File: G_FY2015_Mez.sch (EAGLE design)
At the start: 197 parts, among them IC100 FT232RL, J1 RPI2_GPIO_HOLES, J100 EPL.00.250.NTN, J101 EPL.00.250.NTN, J102 EPL.00.250.NTN, J103 EPL.00.250.NTN, J180 TOKUDEN_SP6, J181 USB Mini-B Connector, J2 SPACEWIRE_MDMMDM9, J300 SHV_PIGTAIL_LAND, J301 SHV_PIGTAIL_LAND, J600_12V IL-4P-S3EN2, J610 2.1MMJACKTHM, U10 LM60, U100 AD9215, U101 AD8138, U102 LM6142, U11 MCP4822-E/SN, U110 AD9215, U111 AD8138, U112 LM6142, U120 AD9215, U121 AD8138, U122 LM6142, U130 AD9215, U131 AD8138, U132 LM6142, U190 SN65LVDS049, U191 GPS_FGPMMOPA6H, U192 LED-5, U300 OPTON_1PA_12, U301 OPTON_1PA_12, U302 2SC1815, U303 2SJ313, U5 MCP3208-CI/SL, U500 LT6106, U510 LT6106, U6 MCP1525TSOT-23-3, U600 PHT12050WAH, U610 PHT12050WAH, U620 LTC1983ES6-3, U7 LM60, U8 LM60, U9 LM60

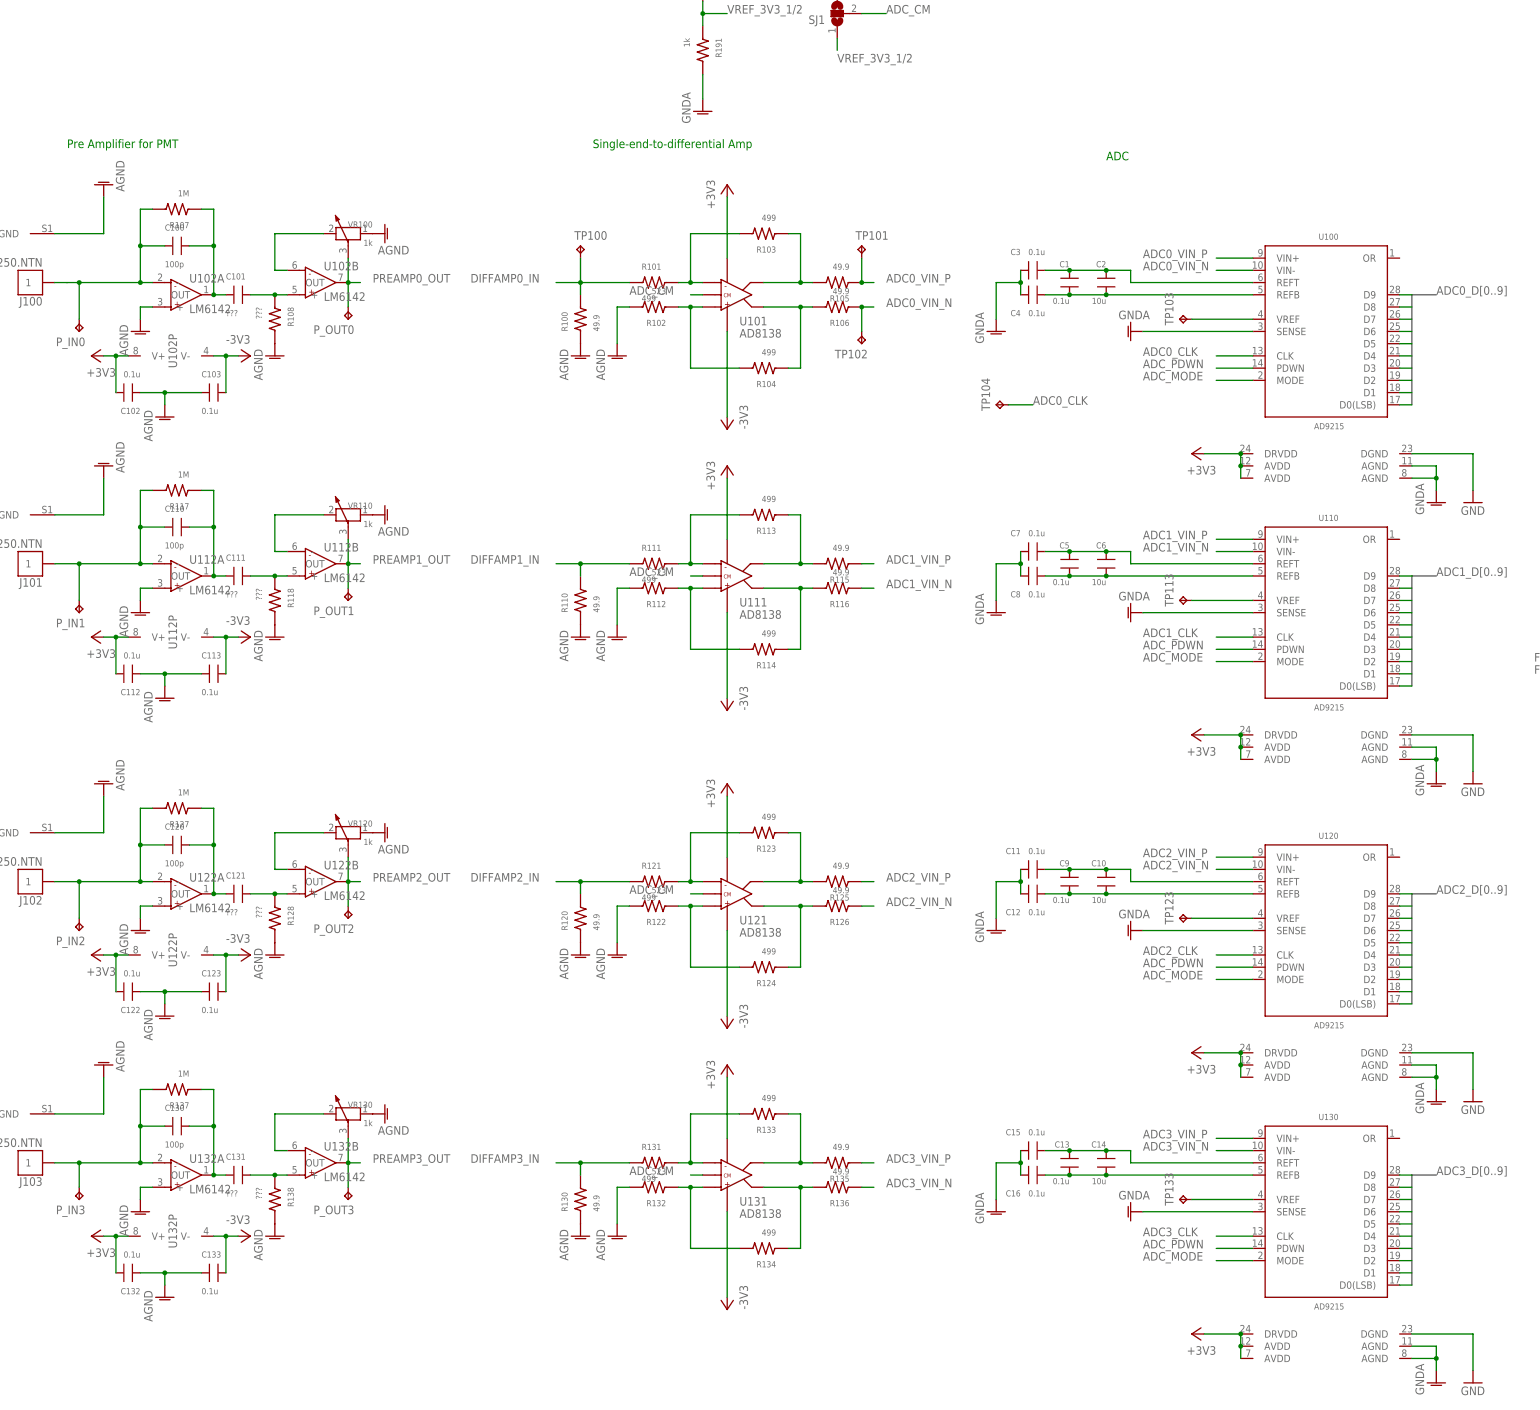
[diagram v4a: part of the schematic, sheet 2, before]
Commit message: GNDA and AGND removed (just use GND)
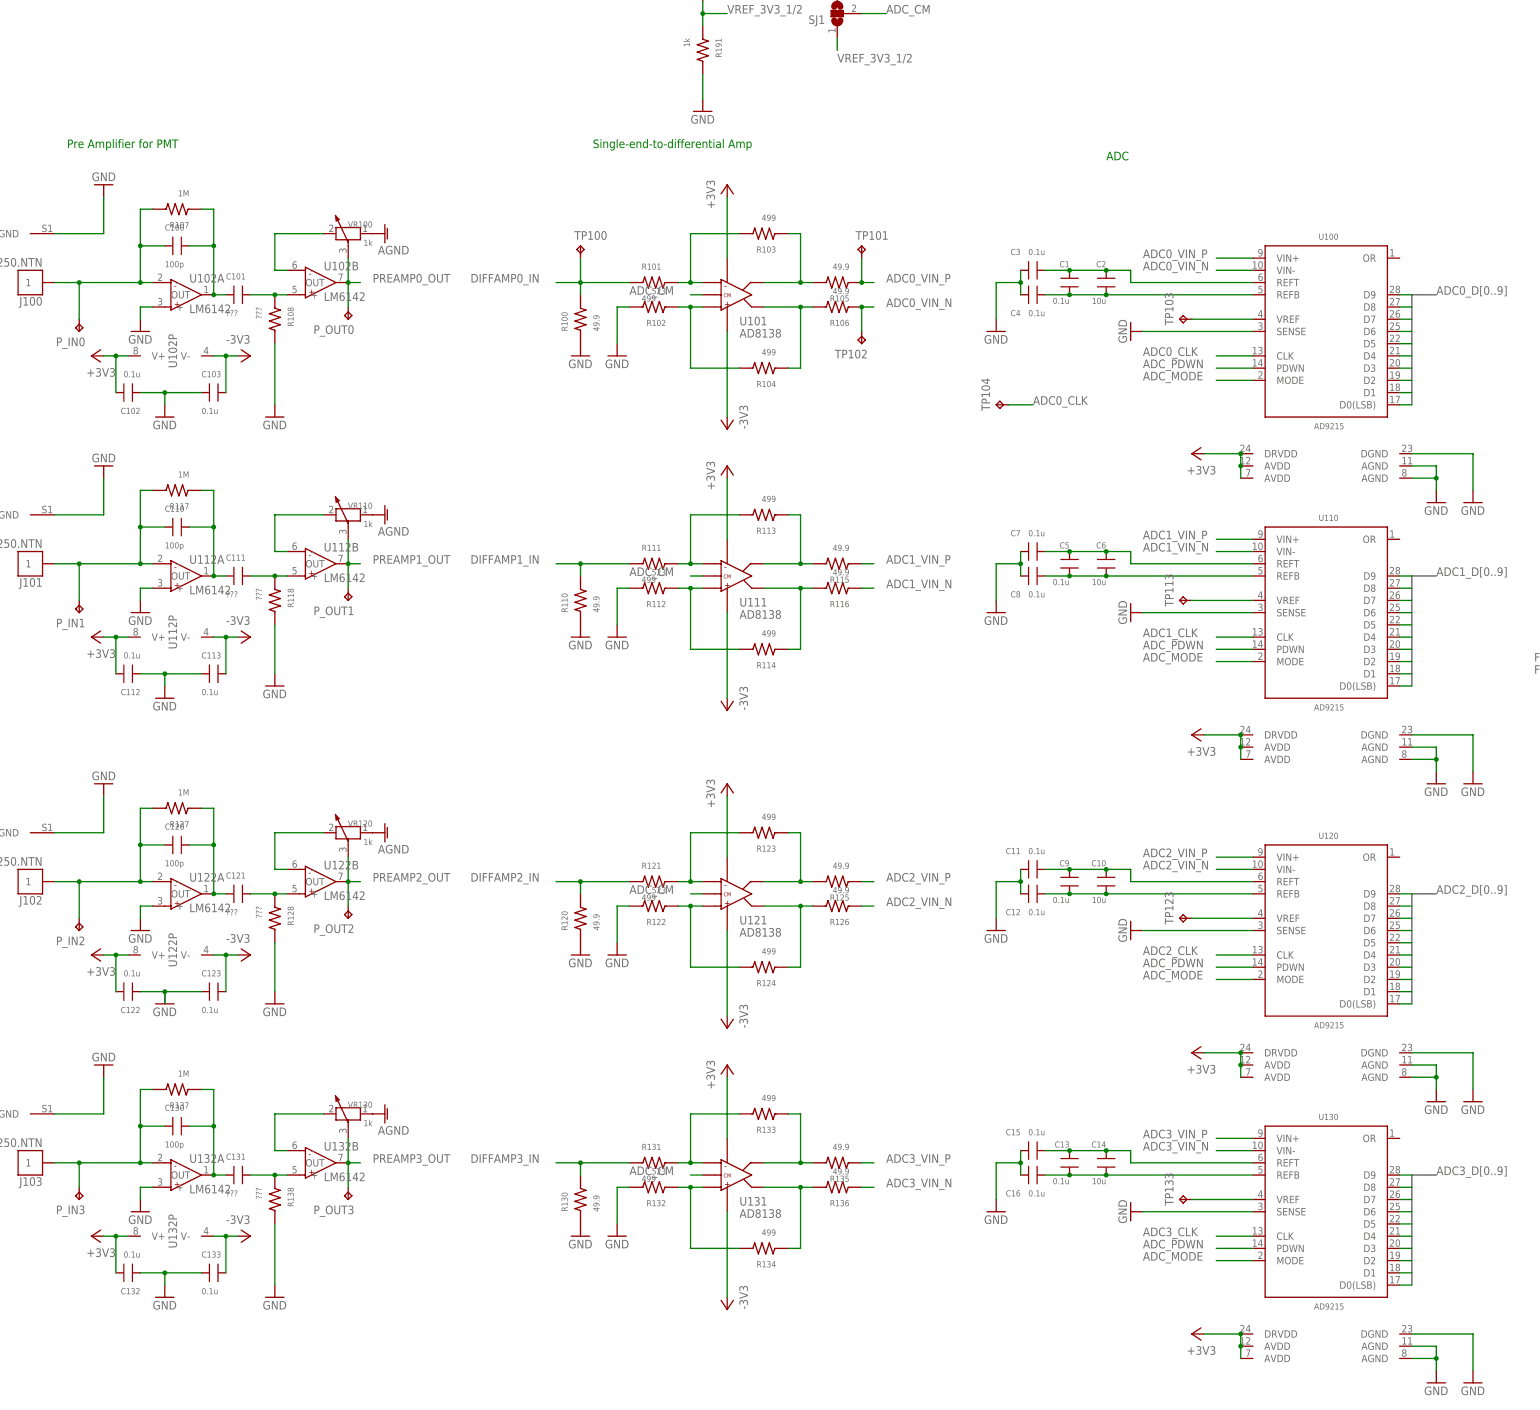
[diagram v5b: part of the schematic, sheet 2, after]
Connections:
- removed net GNDA: C11.2, C12.2, C15.2, C16.2, C3.2, C4.2, C7.2, C8.2, R191.2, U100.AGND@1, U100.AGND@2, U100.SENSE, U110.AGND@1, U110.AGND@2, U110.SENSE, U120.AGND@1, U120.AGND@2, U120.SENSE, U130.AGND@1, U130.AGND@2, U130.SENSE
- net AGND: no longer C102.1, C103.1, C112.1, C113.1, C122.1, C123.1, C132.1, C133.1, C17.1, J100.GND, J101.GND, J102.GND, J103.GND, JP2.2, JP2.4, R100.1, R102.2, R108.2, R110.1, R112.2, R118.2, R120.1, R122.2, R128.2, R130.1, R132.2, R138.2, U10.GND, U102A.+, U112A.+, U122A.+, U132A.+, U5P.AGND, U6.VSS, U7.GND, U8.GND, U9.GND
- net GND: now also C102.1, C103.1, C11.2, C112.1, C113.1, C12.2, C122.1, C123.1, C132.1, C133.1, C15.2, C16.2, C17.1, C3.2, C4.2, C7.2, C8.2, J100.GND, J101.GND, J102.GND, J103.GND, JP2.2, JP2.4, R100.1, R102.2, R108.2, R110.1, R112.2, R118.2, R120.1, R122.2, R128.2, R130.1, R132.2, R138.2, R191.2, U10.GND, U100.AGND@1, U100.AGND@2, U100.SENSE, U102A.+, U110.AGND@1, U110.AGND@2, U110.SENSE, U112A.+, U120.AGND@1, U120.AGND@2, U120.SENSE, U122A.+, U130.AGND@1, U130.AGND@2, U130.SENSE, U132A.+, U5P.AGND, U6.VSS, U7.GND, U8.GND, U9.GND
